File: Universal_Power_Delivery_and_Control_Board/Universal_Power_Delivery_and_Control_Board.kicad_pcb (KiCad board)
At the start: 4 copper layers, 99.5 x 99.5 mm, 137 parts, among them CN1 B03B-XASK-1-A(LF)(SN), CN2 B03B-XASK-1-A(LF)(SN), CN3 B03B-XASK-1-A(LF)(SN), CN4 B03B-XASK-1-A(LF)(SN), SW2 TS1102-TD35HBM, U1 TPS259470LRPWR, U10 SN74LVC1G17DCKR, U11 SN74LVC1G17DCKR, U12 SN74LVC1G17DCKR, U13 SN74LVC1G17DCKR, U14 SN74LVC1G17DCKR, U15 SN74LVC541APWR_C113281, U16 SN74LVC541APWR_C113281, U17 SN74LVC1G17DCKR, U18 LM66200DRLR, U19 TF-0803-0, U2 CH224Q_C46061833, U20 TCA9555PWR, U21 TPS22919DCK, U22 HC-PM254-8.5H-2X4PW-02A, U3 USBLC6-2SC6, U4 ESD2CAN24-ES, U5 S2B-ZR (LF)(SN), U6 USBLC6-2SC6, U7 TPS54202DDC, U8 TPS51385RJNR, U9 TPS24751RUVR

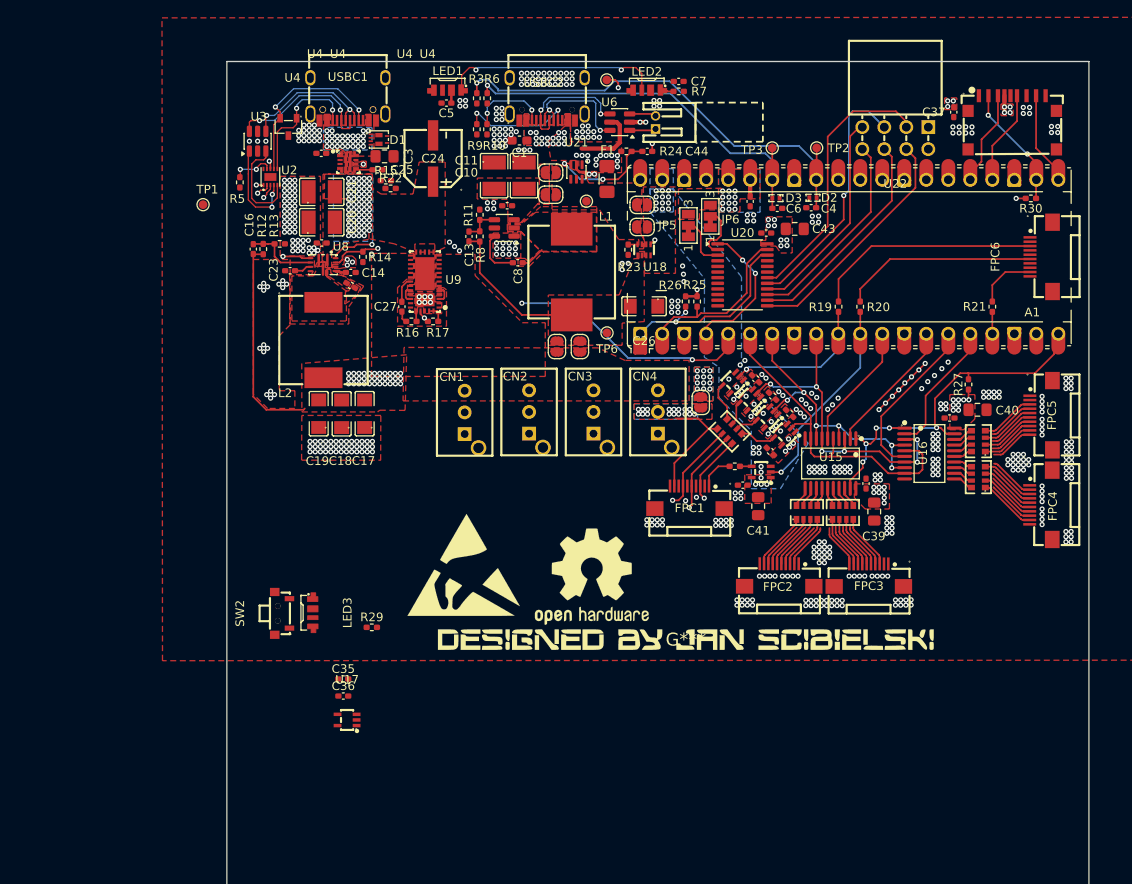
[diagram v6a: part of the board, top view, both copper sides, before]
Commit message: Practically finished layout, need to route the buttons.
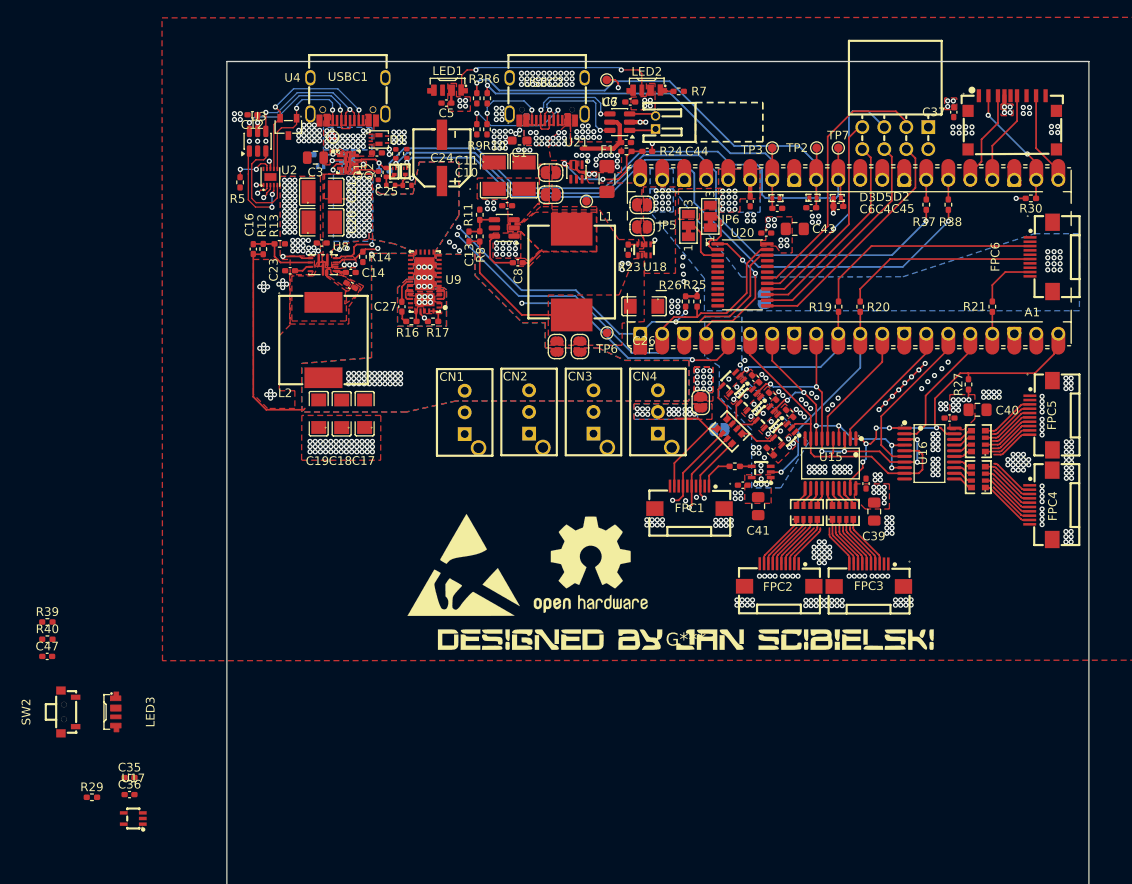
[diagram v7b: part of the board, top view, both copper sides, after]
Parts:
- added C12: 100nF, Capacitor_SMD:C_0402_1005Metric_Pad0.74x0.62mm_HandSolder, F.Cu at (105.1, 44.4)
- added C45: 10nF, Capacitor_SMD:C_0402_1005Metric_Pad0.74x0.62mm_HandSolder, F.Cu at (172.7, 54.9)
- added C46: 100nF, Capacitor_SMD:C_0402_1005Metric_Pad0.74x0.62mm_HandSolder, F.Cu at (148.2, 47.5)
- added C47: 100nF, Capacitor_SMD:C_0402_1005Metric_Pad0.74x0.62mm_HandSolder, F.Cu at (81.4, 106.9)
- added D4: 3.9V, Diode_SMD:D_SOD-882, B.Cu at (113.0, 50.3)
- added D5: PESDNC2FD3V3BS, lcsc_footprints:C496536_DFN1006-2L-BI, F.Cu at (172.6, 54.0)
- added JP11: SolderJumper_2_Open, Jumper:SolderJumper-2_P1.3mm_Open_RoundedPad1.0x1.5mm, B.Cu at (159.0, 80.7)
- added JP3: SolderJumper_2_Open, Jumper:SolderJumper-2_P1.3mm_Open_RoundedPad1.0x1.5mm, B.Cu at (164.2, 65.6)
- added Q1: PMZ600UNEYL, lcsc_footprints:C547286_SOT-883-3_L1_0-W0_6-BR, F.Cu at (121.5, 50.9)
- added Q2: PMZ600UNEYL, lcsc_footprints:C547286_SOT-883-3_L1_0-W0_6-BR, F.Cu at (122.8, 50.9)
- added R28: ?, Resistor_SMD:R_0402_1005Metric, F.Cu at (123.0, 52.5)
- added R31: ?, Resistor_SMD:R_0402_1005Metric_Pad0.72x0.64mm_HandSolder, B.Cu at (112.8, 49.0)
- added R32: ?, Resistor_SMD:R_0402_1005Metric_Pad0.72x0.64mm_HandSolder, B.Cu at (116.0, 48.9)
- added R33: ?, Resistor_SMD:R_0402_1005Metric_Pad0.72x0.64mm_HandSolder, B.Cu at (116.0, 50.8)
- added R34: ?, Resistor_SMD:R_0402_1005Metric_Pad0.72x0.64mm_HandSolder, B.Cu at (116.0, 49.8)
- added R35: 10K, Resistor_SMD:R_0402_1005Metric, F.Cu at (122.9, 48.8)
- added R36: 10K, Resistor_SMD:R_0402_1005Metric, F.Cu at (121.7, 48.9)
- added R37: 1K, Resistor_SMD:R_0402_1005Metric_Pad0.72x0.64mm_HandSolder, F.Cu at (182.9, 54.7)
- added R38: 1K, Resistor_SMD:R_0402_1005Metric_Pad0.72x0.64mm_HandSolder, F.Cu at (185.4, 54.7)
- added R39: 100K, Resistor_SMD:R_0402_1005Metric_Pad0.72x0.64mm_HandSolder, F.Cu at (81.4, 102.9)
- added R4: 10K, Resistor_SMD:R_0402_1005Metric_Pad0.72x0.64mm_HandSolder, B.Cu at (120.3, 50.8)
- added R40: 10K, Resistor_SMD:R_0402_1005Metric_Pad0.72x0.64mm_HandSolder, F.Cu at (81.4, 104.9)
- added TP7: CC1, TestPoint:TestPoint_Pad_D1.0mm, F.Cu at (172.7, 48.2)
- C25: footprint Capacitor_SMD:C_0402_1005Metric_Pad0.74x0.62mm_HandSolder -> Capacitor_SMD:C_0402_1005Metric
- C3: footprint Capacitor_SMD:C_0805_2012Metric_Pad1.18x1.45mm_HandSolder -> Capacitor_SMD:C_0805_2012Metric
- R15, R22: footprint Resistor_SMD:R_0402_1005Metric_Pad0.72x0.64mm_HandSolder -> Resistor_SMD:R_0402_1005Metric
- moved R29 37.8 mm to (86.6, 123.1)
- moved SW2 27.2 mm to (83.8, 113.3)
- moved U17 27.2 mm to (91.3, 125.6)
- moved C35 27.2 mm to (90.9, 120.8)
- moved C36 27.2 mm to (90.9, 122.8)
- moved LED3 25.5 mm to (89.3, 113.3)
- moved TP1 16.9 mm to (114.4, 46.9)
- moved C3 7.98 mm to (112.4, 49.3), turned to 180 degrees
- moved C2 6.43 mm to (119.5, 48.8), turned to 0 degrees
- moved C7 6.08 mm to (148.7, 42.9), turned to 180 degrees
- moved REF** 1.38 mm to (144.2, 96.3)
- moved C24 1.03 mm to (127.0, 49.3)
- moved R15 0.95 mm to (120.6, 51.0), turned to -90 degrees
- moved C25 0.68 mm to (119.6, 51.4), turned to -90 degrees
- moved R22 0.35 mm to (121.1, 52.5)
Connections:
- net /Digital_Signal_Output/CLK renamed /Power_Output/5V_O1
- net /Digital_Signal_Output/LE renamed /Power_Output/5V_O2
- net /Digital_Signal_Output/OE renamed /Power_Output/5V_O3
- A1 pad 26: unconnected-(A1-GPIO20-Pad26) -> /PD_Section/MAX_current
- A1 pad 27: unconnected-(A1-GPIO21-Pad27) -> /PD_Section/H_current
- A1 pad 29: unconnected-(A1-GPIO22-Pad29) -> /PD_Section/IND_LED_DIN
- A1 pad 31: unconnected-(A1-GPIO26_ADC0-Pad31) -> /PD_Section/I_MONITOR
- A1 pad 5: /SS_EN -> unconnected-(A1-GPIO3-Pad5)
- C28 pad 1: +5V_VSYS -> Net-(JP11-A)
- C29 pad 1: +5V_VSYS -> Net-(JP11-A)
- C30 pad 1: +5V_VSYS -> Net-(JP11-A)
- C31 pad 1: +5V_VSYS -> Net-(JP11-A)
- C32 pad 1: +5V_VSYS -> Net-(JP11-A)
- C41 pad 1: GND -> Net-(JP11-A)
- C41 pad 2: +5V_VSYS -> GND
- R17 pad 1: /SS_EN -> /P00
- R22 pad 2: unconnected-(R22-Pad2) -> Net-(Q2-D)
- SW2 pad 1: unconnected-(SW2-Pad1) -> Net-(R40-Pad1)
- SW2 pad 2: unconnected-(SW2-Pad2) -> GND
- SW2 pad 3: unconnected-(SW2-Pad3) -> GND
- SW2 pad 4: unconnected-(SW2-Pad4) -> GND
- U1 pad 1: unconnected-(U1-EN/UVLO-Pad1) -> Net-(D4-K)
- U1 pad 2: unconnected-(U1-OVLO/OVCSEL-Pad2) -> Net-(U1-OVLO/OVCSEL)
- U10 pad 5: +5V_VSYS -> Net-(JP11-A)
- U11 pad 5: +5V_VSYS -> Net-(JP11-A)
- U12 pad 5: +5V_VSYS -> Net-(JP11-A)
- U13 pad 5: +5V_VSYS -> Net-(JP11-A)
- U14 pad 5: +5V_VSYS -> Net-(JP11-A)
- U2 pad 10: /PD_Section/PGOOD -> unconnected-(U2-PG-Pad10)
- U9 pad 33: /SS_EN -> /P00
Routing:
- net Net-(Q2-G): track 0.00 -> 78.2 mm, vias 0 -> 2
- net Net-(Q1-G): track 0.00 -> 77.3 mm, vias 0 -> 2
- net /PD_Section/I_MONITOR: track 0.00 -> 69.1 mm
- net /SCL: track 21.4 -> 89.6 mm, vias 1 -> 3
- net /SDA: track 24.5 -> 89.1 mm, vias 3 -> 5
- net /PD_Section/PG_eFUSE: track 0.00 -> 55.2 mm, vias 0 -> 2
- net /SS_EN: track 41.5 -> 0.00 mm, vias 3 -> 0
- net /P00: track 0.00 -> 41.5 mm, vias 0 -> 3
- net Net-(U1-ILM): track 0.00 -> 4.86 mm, vias 0 -> 1
- net Net-(D4-K): track 0.00 -> 4.29 mm, vias 0 -> 1
- net Net-(U1-OVLO/OVCSEL): track 0.00 -> 3.09 mm, vias 0 -> 1
- net /PD_Section/MAX_current: track 0.00 -> 2.28 mm
- net /PD_Section/H_current: track 0.00 -> 2.28 mm
- net Net-(Q2-D): track 0.00 -> 2.28 mm
- net Net-(Q1-D): track 0.00 -> 2.12 mm
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- added copper zone on In2.Cu, net +12V_PD
- added copper zone on B.Cu, net Net-(JP11-A)
- added copper zone on F.Cu, net Net-(JP11-A)
- added copper zone on B.Cu, net VOUT_connectors
- added copper zone on In2.Cu, net VOUT_connectors
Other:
- board text removed: "U4"

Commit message: Fished layout for now, need to add some components for optional functionality.
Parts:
- removed the G*** at (155.1, 104.9)
- removed JP5, JP6: SolderJumper_3_Bridged12, Jumper:SolderJumper-3_P1.3mm_Bridged12_Pad1.0x1.5mm_NumberLabels
- added C48: 100nF, Capacitor_SMD:C_0402_1005Metric_Pad0.74x0.62mm_HandSolder, F.Cu at (102.5, 123.7)
- added C49: 100nF, Capacitor_SMD:C_0402_1005Metric_Pad0.74x0.62mm_HandSolder, F.Cu at (111.4, 129.6)
- added C50: 100nF, Capacitor_SMD:C_0402_1005Metric_Pad0.74x0.62mm_HandSolder, F.Cu at (102.3, 119.8)
- added C51: 100nF, Capacitor_SMD:C_0402_1005Metric_Pad0.74x0.62mm_HandSolder, F.Cu at (111.4, 119.5)
- added C52: 100nF, Capacitor_SMD:C_0402_1005Metric_Pad0.74x0.62mm_HandSolder, F.Cu at (154.2, 74.8)
- added G***: LOGO, LOGO, F.Cu at (188.6, 137.8)
- added G***: LOGO, LOGO, F.Cu at (137.5, 131.4)
- added G***: LOGO, LOGO, F.Cu at (136.5, 136.2)
- added H1: MountingHole_Pad, MountingHole:MountingHole_2.2mm_M2_Pad_Via, F.Cu at (103.5, 74.1)
- added H2: MountingHole_Pad, MountingHole:MountingHole_2.2mm_M2_Pad_Via, F.Cu at (166.2, 76.5)
- added H3: MountingHole_Pad, MountingHole:MountingHole_2.2mm_M2_Pad_Via, F.Cu at (118.8, 125.8)
- added H4: MountingHole_Pad, MountingHole:MountingHole_2.2mm_M2_Pad_Via, F.Cu at (190.5, 130.2)
- added LED4: SK6812SIDE-A_C5378721, lcsc_footprints:C5378721_LED-SMD_4P-L4_0-W1_6-L, F.Cu at (102.8, 126.8)
- added LED5: SK6812SIDE-A_C5378721, lcsc_footprints:C5378721_LED-SMD_4P-L4_0-W1_6-L, F.Cu at (102.8, 116.8)
- added R41: 100K, Resistor_SMD:R_0402_1005Metric_Pad0.72x0.64mm_HandSolder, F.Cu at (113.9, 128.5)
- added R42: 10K, Resistor_SMD:R_0402_1005Metric_Pad0.72x0.64mm_HandSolder, F.Cu at (111.4, 128.5)
- added R43: 100K, Resistor_SMD:R_0402_1005Metric_Pad0.72x0.64mm_HandSolder, F.Cu at (113.9, 118.5)
- added R44: 10K, Resistor_SMD:R_0402_1005Metric_Pad0.72x0.64mm_HandSolder, F.Cu at (111.4, 118.5)
- added R45: 33R, Resistor_SMD:R_0402_1005Metric_Pad0.72x0.64mm_HandSolder, F.Cu at (165.0, 100.3)
- added R46: 10K, Resistor_SMD:R_0402_1005Metric_Pad0.72x0.64mm_HandSolder, F.Cu at (153.2, 91.8)
- added R47: 10K, Resistor_SMD:R_0402_1005Metric_Pad0.72x0.64mm_HandSolder, F.Cu at (152.4, 97.2)
- added SW3: TS1102-TD35HBM, lcsc_footprints:C36936640_SW-SMD_TS1102-TD35HBM, F.Cu at (108.2, 126.8)
- added SW4: TS1102-TD35HBM, lcsc_footprints:C36936640_SW-SMD_TS1102-TD35HBM, F.Cu at (108.2, 116.8)
- added U23: SN74LVC1G17DCKR, lcsc_footprints:C10425_SC-70-5_L2_1-W1_3-P0_65-LS2_1-BR, F.Cu at (154.7, 73.0)
- moved R39 47.9 mm to (114.0, 138.0), turned to 180 degrees
- moved R40 44.8 mm to (111.5, 138.0)
- moved C47 44.2 mm to (111.6, 139.1)
- moved JP3 35.4 mm to (157.1, 100.2), turned to 90 degrees
- moved SW2 33.9 mm to (108.2, 136.8)
- moved C17 33.0 mm to (116.4, 111.8)
- moved C19 33.0 mm to (111.1, 111.8)
- moved C32 33.0 mm to (160.1, 120.0)
- moved C34 33.0 mm to (183.9, 112.3)
- moved FPC2 33.0 mm to (164.3, 130.4)
- moved JP1 33.0 mm to (138.6, 104.0)
- moved JP2 33.0 mm to (141.3, 104.0)
- moved L2 33.0 mm to (111.7, 103.3)
- moved RN5 33.0 mm to (187.3, 114.9)
- moved U10 33.0 mm to (164.9, 114.2)
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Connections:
- net /Power_Output/5V_O1 renamed /Digital_Signal_Output/CLK
- net /Power_Output/5V_O2 renamed /Digital_Signal_Output/LE
- net /Power_Output/5V_O3 renamed /Digital_Signal_Output/OE
- A1 pad 29: /PD_Section/IND_LED_DIN -> /UI_Section/IND_LED_DIN
- A1 pad 5: unconnected-(A1-GPIO3-Pad5) -> Net-(A1-GPIO3)
- C36 pad 1: Net-(U17-VCC) -> +5V_VSYS
- C36 pad 2: Net-(U17-GND) -> GND
- C47 pad 2: Net-(C47-Pad2) -> /P05
- LED1 pad 3: /PD_Section/IND_LED_DOUT -> unconnected-(LED1-DOUT-Pad3)
- LED3 pad 3: unconnected-(LED3-DOUT-Pad3) -> Net-(LED3-DOUT)
- R14 pad 1: /Power_Output/EN_TPS51385 -> /P02
- R17 pad 1: /P00 -> /P04
- R39 pad 2: Net-(C47-Pad2) -> /P05
- R40 pad 2: Net-(C47-Pad2) -> /P05
- R7 pad 1: /PD_Section/IND_LED_DIN -> Net-(U23-Y)
- U1 pad 3: /PD_Section/PG_eFUSE -> /P00
- U17 pad 2: unconnected-(U17-A-Pad2) -> /Button_LED_DIN
- U17 pad 3: Net-(U17-GND) -> GND
- U17 pad 5: Net-(U17-VCC) -> +5V_VSYS
- U20 pad 10: unconnected-(U20-P06-Pad10) -> /P06
- U20 pad 11: unconnected-(U20-P07-Pad11) -> /P07
- U20 pad 2: Net-(JP6-C) -> GND
- U20 pad 3: Net-(JP5-C) -> GND
- U8 pad 11: /Power_Output/EN_TPS51385 -> /P02
- U8 pad 12: /Power_Output/MODE_TPS51385 -> /P01
- U8 pad 3: /Power_Output/PG_TPS51385 -> /P03
- U9 pad 33: /P00 -> /P04
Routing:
- net /P07: track 0.00 -> 198.7 mm, vias 0 -> 2
- net /P06: track 0.00 -> 194.5 mm, vias 0 -> 2
- net /P05: track 0.00 -> 186.8 mm, vias 0 -> 2
- net +3V3: track 8.29 -> 102.7 mm, vias 57 -> 60
- net /Button_LED_DIN: track 0.00 -> 82.1 mm, vias 0 -> 3
- net /P03: track 0.00 -> 57.7 mm, vias 0 -> 4
- net /PD_Section/PG_eFUSE: track 55.2 -> 0.00 mm, vias 2 -> 0
- net /Digital_Signal_Output/HIGH_CURRENT_EN: track 0.00 -> 53.8 mm, vias 0 -> 4
- net /Power_Output/PG_TPS51385: track 52.7 -> 0.00 mm, vias 4 -> 0
- net /P01: track 0.00 -> 48.5 mm, vias 0 -> 3
- net /P02: track 0.00 -> 47.9 mm, vias 0 -> 3
- net /P04: track 0.00 -> 47.7 mm, vias 0 -> 3
- net /Power_Output/MODE_TPS51385: track 44.4 -> 0.00 mm, vias 3 -> 0
- net /Power_Output/EN_TPS51385: track 43.8 -> 0.00 mm, vias 3 -> 0
- net /UI_Section/IND_LED_DIN: track 0.00 -> 34.2 mm, vias 0 -> 1
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- added copper zone on B.Cu, net GND
- added copper zone on In2.Cu, net Net-(U21-IN)
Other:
- board size 99.5 x 99.5 mm -> 99.5 x 69.3 mm
